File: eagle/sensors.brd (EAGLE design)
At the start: 43 x 70 mm, 14 parts, among them U1 DHT22

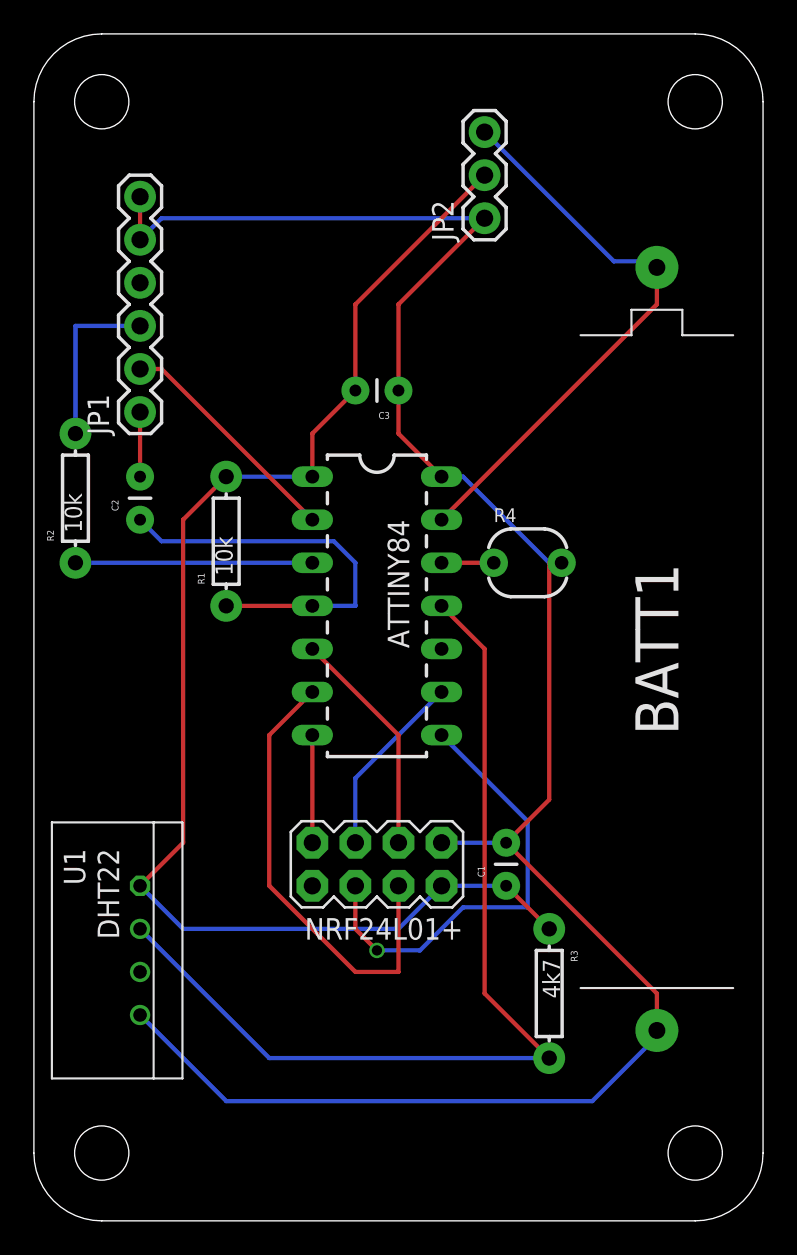
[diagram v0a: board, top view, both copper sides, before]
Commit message: make capacitors bigger
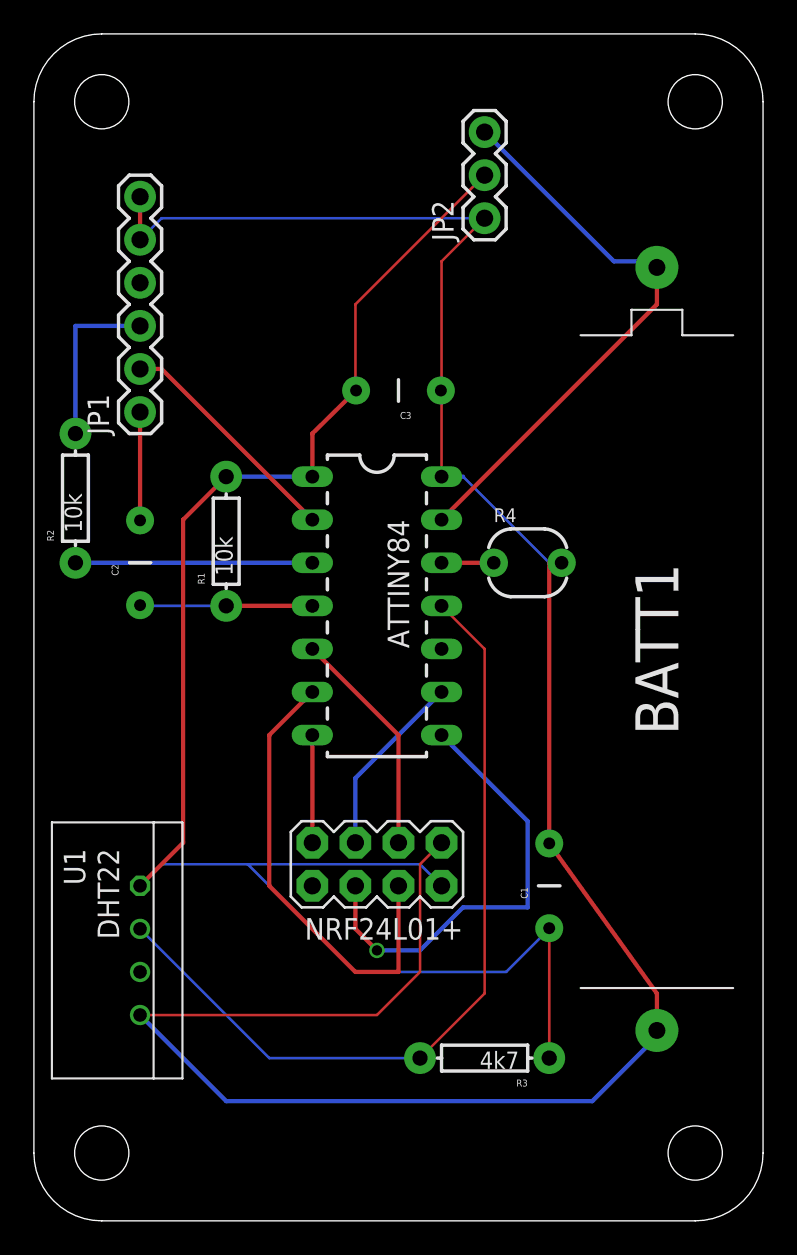
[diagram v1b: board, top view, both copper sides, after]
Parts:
- C1, C2, C3: device SparkFun-Capacitors:CAP-PTH-SMALL -> SparkFun-Capacitors:CAP-PTH-5MM
- moved R3 5.39 mm to (34.3, 14.0), turned to 180 degrees
- moved C1 2.54 mm to (38.1, 24.1)
- moved C2 2.54 mm to (14.0, 43.2)
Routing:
- net VCC: track 80.6 -> 101.4 mm
- net GND: track 122.3 -> 140.0 mm
- net N$3: track 23.9 -> 10.2 mm
- net N$11: track 56.6 -> 49.0 mm
- net N$4: track 3.81 -> 6.39 mm
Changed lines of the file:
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@@
 <element name="R1" library="SparkFun-Resistors" package="AXIAL-0.3EZ" value="10k" x="19.05" y="44.45" rot="R90"/>
 <element name="R2" library="SparkFun-Resistors" package="AXIAL-0.3EZ" value="10k" x="10.16" y="46.99" rot="R90"/>
-<element name="C1" library="SparkFun-Capacitors" package="CAP-PTH-SMALL" value="100n" x="35.56" y="24.13" rot="R90"/>
-<element name="C2" library="SparkFun-Capacitors" package="CAP-PTH-SMALL" value="100n" x="13.97" y="45.72" rot="R90"/>
+<element name="C1" library="SparkFun-Capacitors" package="CAP-PTH-5MM" value="100n" x="38.1" y="24.13" rot="R90"/>
+<element name="C2" library="SparkFun-Capacitors" package="CAP-PTH-5MM" value="100n" x="13.97" y="43.18" rot="R90"/>
 <element name="JP1" library="SparkFun-Connectors" package="1X06" value="FTDI" x="13.97" y="52.07" rot="R90"/>
 <element name="BATT1" library="adafruit" package="12BH412" value="AAA" x="44.45" y="38.1" rot="R90"/>
 <element name="JP2" library="SparkFun-Connectors" package="1X03" value="NCP1402-3.3v" x="34.29" y="63.5" rot="R90"/>
 <element name="NRF24L01+" library="SparkFun-Connectors" package="2X4" value="" x="27.94" y="25.4" rot="R180"/>
-<element name="R3" library="SparkFun-Resistors" package="AXIAL-0.3EZ" value="4k7" x="38.1" y="17.78" rot="R270"/>
+<element name="R3" library="SparkFun-Resistors" package="AXIAL-0.3EZ" value="4k7" x="34.29" y="13.97" rot="R180"/>
 <element name="R4" library="SparkFun-Sensors" package="PHOTOCELL" value="LDR" x="36.83" y="43.18"/>
 <element name="U1" library="RHT03_DHT-22_AM2302" package="RHT03_DHT-22" value="DHT22" x="13.97" y="20.32" rot="R270">
 <attribute name="PROD_ID" value="SEN-10167" x="-13.97" y="0" size="1.778" layer="27" rot="R270" display="off"/>
 </element>
-<element name="C3" library="SparkFun-Capacitors" package="CAP-PTH-SMALL" value="100n" x="29.21" y="53.34" rot="R180"/>
+<element name="C3" library="SparkFun-Capacitors" package="CAP-PTH-5MM" value="100n" x="29.21" y="53.34" rot="R180"/>
 <element name="U$1" library="dp_devices" package="DP7043_V1" value="" x="29.21" y="39.37" rot="R90"/>
 </elements>
@@
 <contactref element="U1" pad="VDD"/>
 <contactref element="R3" pad="P$1"/>
-<wire x1="38.1" y1="21.59" x2="35.56" y2="24.13" width="0.254" layer="1"/>
-<wire x1="16.51" y1="21.59" x2="13.97" y2="24.13" width="0.254" layer="16"/>
-<wire x1="29.21" y1="21.59" x2="16.51" y2="21.59" width="0.254" layer="16"/>
-<wire x1="31.75" y1="24.13" x2="29.21" y2="21.59" width="0.254" layer="16"/>
-<wire x1="31.75" y1="24.13" x2="35.56" y2="24.13" width="0.254" layer="16"/>
 <wire x1="19.05" y1="48.26" x2="24.13" y2="48.26" width="0.254" layer="16"/>
-<wire x1="24.13" y1="50.8" x2="26.67" y2="53.34" width="0.254" layer="1"/>
+<wire x1="24.13" y1="50.8" x2="26.71" y2="53.34" width="0.254" layer="1"/>
 <wire x1="24.13" y1="48.26" x2="24.13" y2="50.8" width="0.254" layer="1"/>
-<wire x1="26.67" y1="58.42" x2="34.29" y2="66.04" width="0.254" layer="1"/>
-<wire x1="26.67" y1="53.34" x2="26.67" y2="58.42" width="0.254" layer="1"/>
 <wire x1="16.51" y1="26.67" x2="13.97" y2="24.13" width="0.254" layer="1"/>
 <wire x1="16.51" y1="45.72" x2="16.51" y2="26.67" width="0.254" layer="1"/>
 <wire x1="19.05" y1="48.26" x2="16.51" y2="45.72" width="0.254" layer="1"/>
+<wire x1="26.67" y1="58.42" x2="34.29" y2="66.04" width="0.1524" layer="1"/>
+<wire x1="26.67" y1="53.34" x2="26.67" y2="58.42" width="0.1524" layer="1"/>
+<wire x1="26.67" y1="53.34" x2="26.71" y2="53.34" width="0.1524" layer="1"/>
+<wire x1="38.1" y1="13.97" x2="38.1" y2="21.63" width="0.1524" layer="1"/>
+<wire x1="30.48" y1="25.4" x2="31.75" y2="24.13" width="0.1524" layer="16"/>
+<wire x1="15.24" y1="25.4" x2="20.32" y2="25.4" width="0.1524" layer="16"/>
+<wire x1="20.32" y1="25.4" x2="30.48" y2="25.4" width="0.1524" layer="16"/>
+<wire x1="13.97" y1="24.13" x2="15.24" y2="25.4" width="0.1524" layer="16"/>
+<wire x1="35.56" y1="19.05" x2="38.1" y2="21.59" width="0.1524" layer="16"/>
+<wire x1="26.67" y1="19.05" x2="35.56" y2="19.05" width="0.1524" layer="16"/>
+<wire x1="20.32" y1="25.4" x2="26.67" y2="19.05" width="0.1524" layer="16"/>
+<wire x1="38.1" y1="21.59" x2="38.1" y2="21.63" width="0.1524" layer="16"/>
 </signal>
 <signal name="N$2">
@@
 <contactref element="NRF24L01+" pad="1"/>
 <contactref element="C3" pad="1"/>
-<wire x1="31.75" y1="26.67" x2="35.56" y2="26.67" width="0.254" layer="16"/>
 <wire x1="19.05" y1="11.43" x2="13.97" y2="16.51" width="0.254" layer="16"/>
 <wire x1="40.64" y1="11.43" x2="19.05" y2="11.43" width="0.254" layer="16"/>
 <wire x1="44.45" y1="15.24" x2="40.64" y2="11.43" width="0.254" layer="16"/>
 <wire x1="44.45" y1="15.24" x2="44.45" y2="15.6" width="0.254" layer="16"/>
-<wire x1="44.45" y1="17.78" x2="35.56" y2="26.67" width="0.254" layer="1"/>
+<wire x1="44.45" y1="17.78" x2="38.1" y2="26.63" width="0.254" layer="1"/>
 <wire x1="44.45" y1="15.6" x2="44.45" y2="17.78" width="0.254" layer="1"/>
 <wire x1="13.97" y1="64.77" x2="13.97" y2="62.23" width="0.254" layer="1"/>
-<wire x1="29.21" y1="50.8" x2="31.75" y2="48.26" width="0.254" layer="1"/>
-<wire x1="29.21" y1="53.34" x2="29.21" y2="50.8" width="0.254" layer="1"/>
-<wire x1="33.02" y1="48.26" x2="38.1" y2="43.18" width="0.254" layer="16"/>
 <wire x1="31.75" y1="48.26" x2="33.02" y2="48.26" width="0.254" layer="16"/>
 <wire x1="38.1" y1="43.18" x2="38.83" y2="43.18" width="0.254" layer="16"/>
-<wire x1="29.21" y1="58.42" x2="34.29" y2="63.5" width="0.254" layer="1"/>
-<wire x1="29.21" y1="53.34" x2="29.21" y2="58.42" width="0.254" layer="1"/>
-<wire x1="15.24" y1="63.5" x2="13.97" y2="62.23" width="0.254" layer="16"/>
-<wire x1="34.29" y1="63.5" x2="15.24" y2="63.5" width="0.254" layer="16"/>
-<wire x1="38.1" y1="29.21" x2="35.56" y2="26.67" width="0.254" layer="1"/>
-<wire x1="38.1" y1="43.18" x2="38.1" y2="29.21" width="0.254" layer="1"/>
+<wire x1="38.1" y1="43.18" x2="38.1" y2="26.63" width="0.254" layer="1"/>
 <wire x1="38.1" y1="43.18" x2="38.83" y2="43.18" width="0.254" layer="1"/>
+<wire x1="39.37" y1="43.18" x2="38.83" y2="43.18" width="0.1524" layer="16"/>
+<wire x1="31.75" y1="53.34" x2="31.75" y2="48.26" width="0.1524" layer="1"/>
+<wire x1="38.1" y1="43.18" x2="33.02" y2="48.26" width="0.1524" layer="16"/>
+<wire x1="30.48" y1="25.4" x2="31.75" y2="26.67" width="0.1524" layer="1"/>
+<wire x1="30.48" y1="19.05" x2="30.48" y2="25.4" width="0.1524" layer="1"/>
+<wire x1="27.94" y1="16.51" x2="30.48" y2="19.05" width="0.1524" layer="1"/>
+<wire x1="13.97" y1="16.51" x2="27.94" y2="16.51" width="0.1524" layer="1"/>
+<wire x1="31.75" y1="60.96" x2="34.29" y2="63.5" width="0.1524" layer="1"/>
+<wire x1="31.75" y1="53.34" x2="31.75" y2="60.96" width="0.1524" layer="1"/>
+<wire x1="31.75" y1="53.34" x2="31.71" y2="53.34" width="0.1524" layer="1"/>
+<wire x1="15.24" y1="63.5" x2="13.97" y2="62.23" width="0.1524" layer="16"/>
+<wire x1="34.29" y1="63.5" x2="15.24" y2="63.5" width="0.1524" layer="16"/>
 </signal>
 <signal name="N$3">
@@
 <contactref element="R1" pad="P$1"/>
 <wire x1="19.05" y1="40.64" x2="24.13" y2="40.64" width="0.254" layer="1"/>
-<wire x1="15.24" y1="44.45" x2="13.97" y2="45.72" width="0.254" layer="16"/>
-<wire x1="25.4" y1="44.45" x2="15.24" y2="44.45" width="0.254" layer="16"/>
-<wire x1="26.67" y1="43.18" x2="25.4" y2="44.45" width="0.254" layer="16"/>
-<wire x1="26.67" y1="40.64" x2="26.67" y2="43.18" width="0.254" layer="16"/>
-<wire x1="24.13" y1="40.64" x2="26.67" y2="40.64" width="0.254" layer="16"/>
+<wire x1="19.05" y1="40.64" x2="13.97" y2="40.64" width="0.1524" layer="16"/>
+<wire x1="13.97" y1="40.64" x2="13.97" y2="40.68" width="0.1524" layer="16"/>
 </signal>
 <signal name="N$4">
 <contactref element="C2" pad="2"/>
 <contactref element="JP1" pad="1"/>
-<wire x1="13.97" y1="52.07" x2="13.97" y2="48.26" width="0.254" layer="1"/>
+<wire x1="13.97" y1="52.07" x2="13.97" y2="45.68" width="0.254" layer="1"/>
 </signal>
 <signal name="N$5">
@@
 <contactref element="R3" pad="P$2"/>
 <contactref element="U1" pad="DATA"/>
-<wire x1="21.59" y1="13.97" x2="13.97" y2="21.59" width="0.254" layer="16"/>
-<wire x1="38.1" y1="13.97" x2="21.59" y2="13.97" width="0.254" layer="16"/>
-<wire x1="34.29" y1="38.1" x2="31.75" y2="40.64" width="0.254" layer="1"/>
-<wire x1="34.29" y1="17.78" x2="34.29" y2="38.1" width="0.254" layer="1"/>
-<wire x1="38.1" y1="13.97" x2="34.29" y2="17.78" width="0.254" layer="1"/>
+<wire x1="21.59" y1="13.97" x2="13.97" y2="21.59" width="0.1524" layer="16"/>
+<wire x1="30.48" y1="13.97" x2="21.59" y2="13.97" width="0.1524" layer="16"/>
+<wire x1="34.29" y1="38.1" x2="31.75" y2="40.64" width="0.1524" layer="1"/>
+<wire x1="34.29" y1="17.78" x2="34.29" y2="38.1" width="0.1524" layer="1"/>
+<wire x1="30.48" y1="13.97" x2="34.29" y2="17.78" width="0.1524" layer="1"/>
 </signal>
 <signal name="N$13">

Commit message: board layout v1.1
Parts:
- moved R4 11.4 mm to (31.8, 53.3)
- moved C3 7.62 mm to (21.6, 53.3)
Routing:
- net N$10: track 3.08 -> 13.9 mm
- net GND: track 140.0 -> 148.6 mm
- net VCC: track 101.4 -> 104.9 mm
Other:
- board text added: "tinysensor 1.1"
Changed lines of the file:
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@@
 <?xml version="1.0" encoding="utf-8"?>
 <!DOCTYPE eagle SYSTEM "eagle.dtd">
-<eagle version="6.5.0">
+<eagle version="7.5.0">
 <drawing>
 <settings>
@@
 <board>
 <plain>
+<text x="29.21" y="7.62" size="1.778" layer="21" rot="R180" align="center">tinysensor 1.1</text>
 </plain>
 <attributes>
@@
 </class>
 </classes>
-<designrules name="SeeedStudio_DRU_no_angle_20130527">
+<designrules name="SeeedStudio_2layer_DRU_no_angle_20140221">
 <description language="de">&lt;b&gt;EAGLE Design Rules&lt;/b&gt;
 &lt;p&gt;
@@
 <description language="zh">&lt;b&gt;Seeed Studio EAGLE Design Rules&lt;/b&gt;
 </description>
-<param name="layerSetup" value="(1*2*15*16)"/>
+<param name="layerSetup" value="(1*16)"/>
 <param name="mtCopper" value="0.035mm 0.0175mm 0.035mm 0.035mm 0.035mm 0.035mm 0.035mm 0.035mm 0.035mm 0.035mm 0.035mm 0.035mm 0.035mm 0.035mm 0.0175mm 0.035mm"/>
-<param name="mtIsolate" value="0.2mm 1.1mm 0.2mm 0.15mm 0.2mm 0.15mm 0.2mm 0.15mm 0.2mm 0.15mm 0.2mm 0.15mm 0.2mm 0.15mm 0.2mm"/>
+<param name="mtIsolate" value="1.5mm 1.1mm 0.2mm 0.15mm 0.2mm 0.15mm 0.2mm 0.15mm 0.2mm 0.15mm 0.2mm 0.15mm 0.2mm 0.15mm 0.2mm"/>
 <param name="mdWireWire" value="6mil"/>
 <param name="mdWirePad" value="6mil"/>
@@
 <param name="rvMicroViaOuter" value="0.25"/>
 <param name="rvMicroViaInner" value="0.25"/>
-<param name="rlMinPadTop" value="6mil"/>
+<param name="rlMinPadTop" value="10mil"/>
 <param name="rlMaxPadTop" value="20mil"/>
-<param name="rlMinPadInner" value="6mil"/>
+<param name="rlMinPadInner" value="10mil"/>
 <param name="rlMaxPadInner" value="20mil"/>
-<param name="rlMinPadBottom" value="6mil"/>
+<param name="rlMinPadBottom" value="10mil"/>
 <param name="rlMaxPadBottom" value="20mil"/>
 <param name="rlMinViaOuter" value="6mil"/>
@@
 <param name="mlMinCreamFrame" value="0mil"/>
 <param name="mlMaxCreamFrame" value="0mil"/>
-<param name="mlViaStopLimit" value="25mil"/>
+<param name="mlViaStopLimit" value="100mil"/>
 <param name="srRoundness" value="0"/>
 <param name="srMinRoundness" value="0mil"/>
@@
 <pass name="Default">
 <param name="RoutingGrid" value="50mil"/>
+<param name="AutoGrid" value="1"/>
+<param name="Efforts" value="0"/>
+<param name="TopRouterVariant" value="1"/>
 <param name="tpViaShape" value="round"/>
 <param name="PrefDir.1" value="|"/>
@@
 <element name="NRF24L01+" library="SparkFun-Connectors" package="2X4" value="" x="27.94" y="25.4" rot="R180"/>
 <element name="R3" library="SparkFun-Resistors" package="AXIAL-0.3EZ" value="4k7" x="34.29" y="13.97" rot="R180"/>
-<element name="R4" library="SparkFun-Sensors" package="PHOTOCELL" value="LDR" x="36.83" y="43.18"/>
+<element name="R4" library="SparkFun-Sensors" package="PHOTOCELL" value="LDR" x="31.75" y="53.34"/>
 <element name="U1" library="RHT03_DHT-22_AM2302" package="RHT03_DHT-22" value="DHT22" x="13.97" y="20.32" rot="R270">
 <attribute name="PROD_ID" value="SEN-10167" x="-13.97" y="0" size="1.778" layer="27" rot="R270" display="off"/>
 </element>
-<element name="C3" library="SparkFun-Capacitors" package="CAP-PTH-5MM" value="100n" x="29.21" y="53.34" rot="R180"/>
+<element name="C3" library="SparkFun-Capacitors" package="CAP-PTH-5MM" value="100n" x="21.59" y="53.34" rot="R180"/>
 <element name="U$1" library="dp_devices" package="DP7043_V1" value="" x="29.21" y="39.37" rot="R90"/>
 </elements>
@@
 <contactref element="R3" pad="P$1"/>
 <wire x1="19.05" y1="48.26" x2="24.13" y2="48.26" width="0.254" layer="16"/>
-<wire x1="24.13" y1="50.8" x2="26.71" y2="53.34" width="0.254" layer="1"/>
-<wire x1="24.13" y1="48.26" x2="24.13" y2="50.8" width="0.254" layer="1"/>
 <wire x1="16.51" y1="26.67" x2="13.97" y2="24.13" width="0.254" layer="1"/>
 <wire x1="16.51" y1="45.72" x2="16.51" y2="26.67" width="0.254" layer="1"/>
 <wire x1="19.05" y1="48.26" x2="16.51" y2="45.72" width="0.254" layer="1"/>
-<wire x1="26.67" y1="58.42" x2="34.29" y2="66.04" width="0.1524" layer="1"/>
-<wire x1="26.67" y1="53.34" x2="26.67" y2="58.42" width="0.1524" layer="1"/>
-<wire x1="26.67" y1="53.34" x2="26.71" y2="53.34" width="0.1524" layer="1"/>
 <wire x1="38.1" y1="13.97" x2="38.1" y2="21.63" width="0.1524" layer="1"/>
 <wire x1="30.48" y1="25.4" x2="31.75" y2="24.13" width="0.1524" layer="16"/>
@@
 <wire x1="20.32" y1="25.4" x2="26.67" y2="19.05" width="0.1524" layer="16"/>
 <wire x1="38.1" y1="21.59" x2="38.1" y2="21.63" width="0.1524" layer="16"/>
+<wire x1="19.1209" y1="48.4277" x2="19.1209" y2="53.2526" width="0.1524" layer="16"/>
+<wire x1="19.1209" y1="53.2526" x2="19.09" y2="53.34" width="0.1524" layer="16"/>
+<wire x1="19.1209" y1="48.4277" x2="19.05" y2="48.26" width="0.1524" layer="16"/>
+<wire x1="31.6299" y1="65.9403" x2="34.1317" y2="65.9403" width="0.1524" layer="1"/>
+<wire x1="19.1209" y1="53.4313" x2="31.6299" y2="65.9403" width="0.1524" layer="1"/>
+<wire x1="34.1317" y1="65.9403" x2="34.29" y2="66.04" width="0.1524" layer="1"/>
+<wire x1="19.1209" y1="53.4313" x2="19.09" y2="53.34" width="0.1524" layer="1"/>
 </signal>
 <signal name="N$2">
@@
 <contactref element="JP2" pad="1"/>
 <contactref element="U1" pad="GND"/>
-<contactref element="R4" pad="2"/>
 <contactref element="NRF24L01+" pad="1"/>
 <contactref element="C3" pad="1"/>
@@
 <wire x1="13.97" y1="64.77" x2="13.97" y2="62.23" width="0.254" layer="1"/>
 <wire x1="31.75" y1="48.26" x2="33.02" y2="48.26" width="0.254" layer="16"/>
-<wire x1="38.1" y1="43.18" x2="38.83" y2="43.18" width="0.254" layer="16"/>
-<wire x1="38.1" y1="43.18" x2="38.1" y2="26.63" width="0.254" layer="1"/>
-<wire x1="38.1" y1="43.18" x2="38.83" y2="43.18" width="0.254" layer="1"/>
-<wire x1="39.37" y1="43.18" x2="38.83" y2="43.18" width="0.1524" layer="16"/>
-<wire x1="31.75" y1="53.34" x2="31.75" y2="48.26" width="0.1524" layer="1"/>
-<wire x1="38.1" y1="43.18" x2="33.02" y2="48.26" width="0.1524" layer="16"/>
 <wire x1="30.48" y1="25.4" x2="31.75" y2="26.67" width="0.1524" layer="1"/>
 <wire x1="30.48" y1="19.05" x2="30.48" y2="25.4" width="0.1524" layer="1"/>
 <wire x1="27.94" y1="16.51" x2="30.48" y2="19.05" width="0.1524" layer="1"/>
 <wire x1="13.97" y1="16.51" x2="27.94" y2="16.51" width="0.1524" layer="1"/>
-<wire x1="31.75" y1="60.96" x2="34.29" y2="63.5" width="0.1524" layer="1"/>
-<wire x1="31.75" y1="53.34" x2="31.75" y2="60.96" width="0.1524" layer="1"/>
-<wire x1="31.75" y1="53.34" x2="31.71" y2="53.34" width="0.1524" layer="1"/>
 <wire x1="15.24" y1="63.5" x2="13.97" y2="62.23" width="0.1524" layer="16"/>
-<wire x1="34.29" y1="63.5" x2="15.24" y2="63.5" width="0.1524" layer="16"/>
+<wire x1="34.29" y1="63.5" x2="24.1245" y2="63.5" width="0.1524" layer="16"/>
+<wire x1="24.1245" y1="63.5" x2="15.24" y2="63.5" width="0.1524" layer="16"/>
+<wire x1="24.1245" y1="63.5" x2="24.1245" y2="53.4313" width="0.1524" layer="16"/>
+<wire x1="24.1245" y1="53.4313" x2="24.09" y2="53.34" width="0.1524" layer="16"/>
+<wire x1="26.805" y1="53.2526" x2="24.1245" y2="53.2526" width="0.1524" layer="1"/>
+<wire x1="31.6299" y1="48.4277" x2="26.805" y2="53.2526" width="0.1524" layer="1"/>
+<wire x1="24.1245" y1="53.2526" x2="24.09" y2="53.34" width="0.1524" layer="1"/>
+<wire x1="31.6299" y1="48.4277" x2="31.75" y2="48.26" width="0.1524" layer="1"/>
+<contactref element="R4" pad="2"/>
+<wire x1="38.1" y1="26.67" x2="38.1" y2="26.805" width="0.4064" layer="16"/>
+<wire x1="38.1" y1="26.805" x2="38.1" y2="43.18" width="0.4064" layer="16"/>
+<wire x1="38.1" y1="43.18" x2="33.7743" y2="48.26" width="0.4064" layer="16"/>
+<wire x1="33.7743" y1="48.26" x2="31.75" y2="48.26" width="0.4064" layer="16"/>
+<wire x1="33.7743" y1="48.26" x2="33.7743" y2="53.2526" width="0.1524" layer="16"/>
+<wire x1="33.7743" y1="53.2526" x2="33.75" y2="53.34" width="0.1524" layer="16"/>
+<wire x1="38.2418" y1="26.805" x2="38.1" y2="26.805" width="0.1524" layer="16"/>
+<wire x1="38.2418" y1="26.805" x2="38.1" y2="26.63" width="0.1524" layer="16"/>
 </signal>
 <signal name="N$3">
@@
 <contactref element="R4" pad="1"/>
 <contactref element="ATTINY84" pad="12"/>
-<wire x1="34.83" y1="43.18" x2="31.75" y2="43.18" width="0.254" layer="1"/>
+<wire x1="29.8429" y1="53.2526" x2="29.75" y2="53.34" width="0.1524" layer="16"/>
+<wire x1="31.75" y1="43.18" x2="29.21" y2="43.18" width="0.254" layer="16"/>
+<wire x1="29.21" y1="43.18" x2="27.94" y2="44.45" width="0.254" layer="16"/>
+<wire x1="27.94" y1="44.45" x2="27.94" y2="52.07" width="0.254" layer="16"/>
+<wire x1="27.94" y1="52.07" x2="29.21" y2="53.34" width="0.254" layer="16"/>
+<wire x1="29.21" y1="53.34" x2="29.75" y2="53.34" width="0" layer="19" extent="16-16"/>
 </signal>
 <signal name="N$11">
@@
 </signal>
 </signals>
+<errors>
+</errors>
 </board>
 </drawing>
